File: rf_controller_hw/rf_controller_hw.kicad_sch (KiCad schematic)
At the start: 9 parts, among them J1 NRF24L01, SW1 SW_Push, SW10 JOYSTICK_BUTTON, SW2 SW_Push, SW3 SW_Push, SW4 SW_Push, SW8 SW_DIP_x05

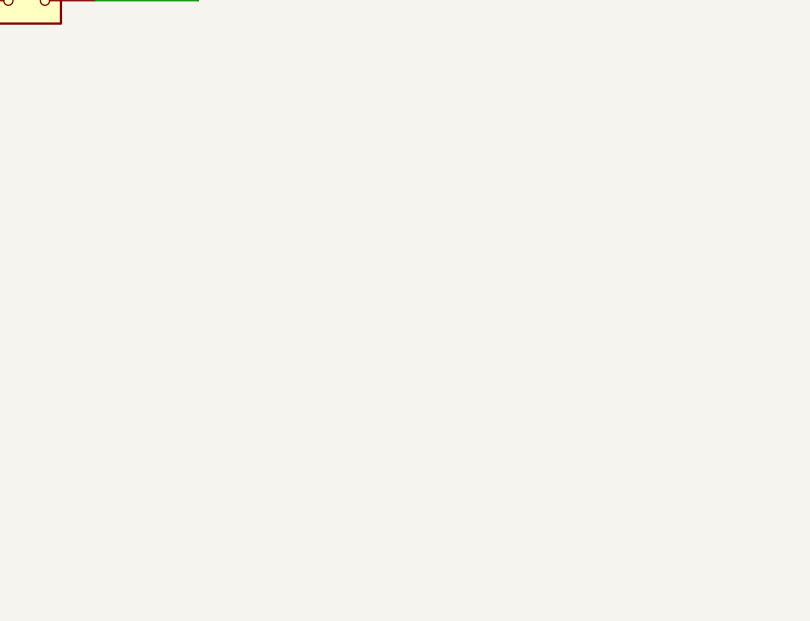
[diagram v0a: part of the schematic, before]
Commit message: Changed to mechanical keyboard switches
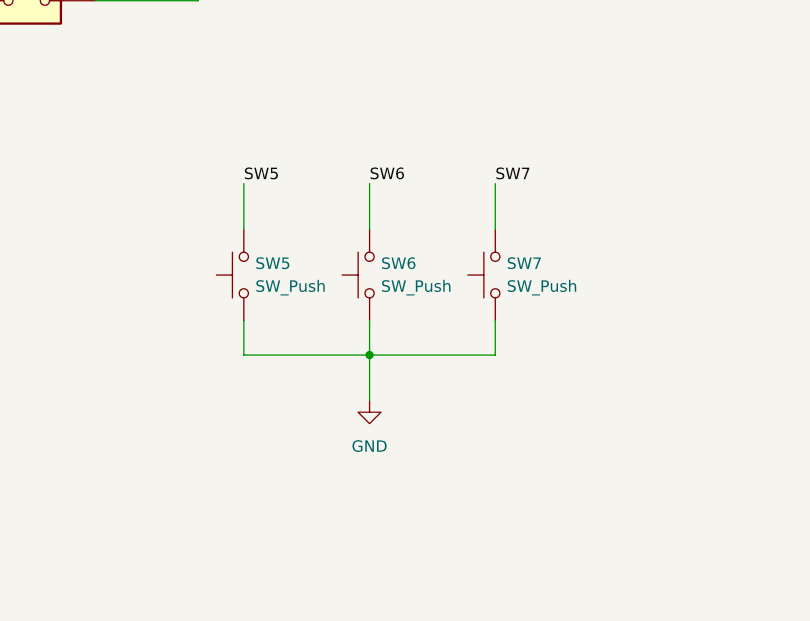
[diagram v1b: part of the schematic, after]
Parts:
- added SW5, SW6, SW7: SW_Push, Button_Switch_Keyboard:SW_Cherry_MX_1.00u_PCB, symbol Switch:SW_Push
- SW1, SW2, SW3, SW4: footprint (none) -> Button_Switch_Keyboard:SW_Cherry_MX_1.00u_PCB
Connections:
- net GND: now also SW5.1, SW6.1, SW7.1
- net SW5: now also SW5.2
- net SW6: now also SW6.2
- net SW7: now also SW7.2
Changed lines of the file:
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@@
   (junction (at 56.007 179.07) (diameter 0) (color 0 0 0 0)
+  )
+  (junction (at 171.45 143.51) (diameter 0) (color 0 0 0 0)
   )
   (junction (at 129.54 52.07) (diameter 0) (color 0 0 0 0)
@@
     (stroke (width 0) (type default) (color 0 0 0 0))
   )
+  (wire (pts (xy 171.45 143.51) (xy 185.42 143.51))
+    (stroke (width 0) (type default) (color 0 0 0 0))
+  )
   (wire (pts (xy 129.54 45.72) (xy 151.13 45.72))
     (stroke (width 0) (type default) (color 0 0 0 0))
@@
     (stroke (width 0) (type default) (color 0 0 0 0))
   )
+  (wire (pts (xy 171.45 139.7) (xy 171.45 143.51))
+    (stroke (width 0) (type default) (color 0 0 0 0))
+  )
   (wire (pts (xy 55.88 139.7) (xy 55.88 137.16))
     (stroke (width 0) (type default) (color 0 0 0 0))
@@
     (stroke (width 0) (type default) (color 0 0 0 0))
   )
+  (wire (pts (xy 185.42 124.46) (xy 185.42 129.54))
+    (stroke (width 0) (type default) (color 0 0 0 0))
+  )
   (wire (pts (xy 140.97 101.6) (xy 152.4 101.6))
     (stroke (width 0) (type default) (color 0 0 0 0))
@@
     (stroke (width 0) (type default) (color 0 0 0 0))
   )
+  (wire (pts (xy 185.42 143.51) (xy 185.42 139.7))
+    (stroke (width 0) (type default) (color 0 0 0 0))
+  )
   (wire (pts (xy 69.85 101.6) (xy 82.55 101.6))
     (stroke (width 0) (type default) (color 0 0 0 0))
@@
     (stroke (width 0) (type default) (color 0 0 0 0))
   )
+  (wire (pts (xy 171.45 148.59) (xy 171.45 143.51))
+    (stroke (width 0) (type default) (color 0 0 0 0))
+  )
   (wire (pts (xy 48.26 179.07) (xy 48.26 165.1))
     (stroke (width 0) (type default) (color 0 0 0 0))
@@
     (stroke (width 0) (type default) (color 0 0 0 0))
   )
+  (wire (pts (xy 157.48 124.46) (xy 157.48 129.54))
+    (stroke (width 0) (type default) (color 0 0 0 0))
+  )
   (wire (pts (xy 129.54 45.72) (xy 129.54 36.83))
     (stroke (width 0) (type default) (color 0 0 0 0))
@@
     (stroke (width 0) (type default) (color 0 0 0 0))
   )
+  (wire (pts (xy 171.45 143.51) (xy 157.48 143.51))
+    (stroke (width 0) (type default) (color 0 0 0 0))
+  )
   (wire (pts (xy 68.58 76.2) (xy 68.58 86.36))
     (stroke (width 0) (type default) (color 0 0 0 0))
@@
     (stroke (width 0) (type default) (color 0 0 0 0))
   )
+  (wire (pts (xy 157.48 143.51) (xy 157.48 139.7))
+    (stroke (width 0) (type default) (color 0 0 0 0))
+  )
   (wire (pts (xy 143.51 49.53) (xy 151.13 49.53))
     (stroke (width 0) (type default) (color 0 0 0 0))
@@
   )
   (wire (pts (xy 140.97 96.52) (xy 152.4 96.52))
+    (stroke (width 0) (type default) (color 0 0 0 0))
+  )
+  (wire (pts (xy 171.45 124.46) (xy 171.45 129.54))
     (stroke (width 0) (type default) (color 0 0 0 0))
   )
@@
     (effects (font (size 1.27 1.27)) (justify left bottom))
   )
+  (label "SW7" (at 185.42 124.46 0)
+    (effects (font (size 1.27 1.27)) (justify left bottom))
+  )
+  (label "SW6" (at 171.45 124.46 0)
+    (effects (font (size 1.27 1.27)) (justify left bottom))
+  )
   (label "SW4" (at 74.93 166.37 0)
     (effects (font (size 1.27 1.27)) (justify left bottom))
@@
   )
   (label "SW2" (at 74.93 151.13 0)
+    (effects (font (size 1.27 1.27)) (justify left bottom))
+  )
+  (label "SW5" (at 157.48 124.46 0)
     (effects (font (size 1.27 1.27)) (justify left bottom))
   )
@@
     (pin "1")
   )
+  (symbol (lib_id "Switch:SW_Push") (at 157.48 134.62 90) (unit 1)
+    (in_bom yes) (on_board yes)
+    (property "Reference" "SW5" (id 0) (at 158.75 133.3499 90)
+      (effects (font (size 1.27 1.27)) (justify right))
+    )
+    (property "Value" "SW_Push" (id 1) (at 158.75 135.8899 90)
+      (effects (font (size 1.27 1.27)) (justify right))
+    )
+    (property "Footprint" "Button_Switch_Keyboard:SW_Cherry_MX_1.00u_PCB" (id 2) (at 152.4 134.62 0)
+      (effects (font (size 1.27 1.27)) hide)
+    )
+    (property "Datasheet" "~" (id 3) (at 152.4 134.62 0)
+      (effects (font (size 1.27 1.27)) hide)
+    )
+    (pin "1")
+    (pin "2")
+  )
   (symbol (lib_id "Device:Battery") (at 238.76 92.71 0) (unit 1)
     (in_bom yes) (on_board yes) (fields_autoplaced)
@@
       (effects (font (size 1.27 1.27)) (justify right))
     )
-    (property "Footprint" "" (id 2) (at 50.8 172.72 0)
+    (property "Footprint" "Button_Switch_Keyboard:SW_Cherry_MX_1.00u_PCB" (id 2) (at 50.8 172.72 0)
       (effects (font (size 1.27 1.27)) hide)
     )
@@
       (effects (font (size 1.27 1.27)) (justify right))
     )
-    (property "Footprint" "" (id 2) (at 57.15 160.02 0)
+    (property "Footprint" "Button_Switch_Keyboard:SW_Cherry_MX_1.00u_PCB" (id 2) (at 57.15 160.02 0)
       (effects (font (size 1.27 1.27)) hide)
     )
@@
     (pin "1")
   )
+  (symbol (lib_id "power:GND") (at 171.45 148.59 0) (unit 1)
+    (in_bom yes) (on_board yes) (fields_autoplaced)
+    (property "Reference" "#PWR?" (id 0) (at 171.45 154.94 0)
+      (effects (font (size 1.27 1.27)) hide)
+    )
+    (property "Value" "GND" (id 1) (at 171.45 153.67 0))
+    (property "Footprint" "" (id 2) (at 171.45 148.59 0)
+      (effects (font (size 1.27 1.27)) hide)
+    )
+    (property "Datasheet" "" (id 3) (at 171.45 148.59 0)
+      (effects (font (size 1.27 1.27)) hide)
+    )
+    (pin "1")
+  )
   (symbol (lib_id "rf_controller_hw:JOYSTICK_BUTTON") (at 167.64 41.91 0) (unit 1)
     (in_bom yes) (on_board yes) (fields_autoplaced)
@@
     (pin "1")
   )
+  (symbol (lib_id "Switch:SW_Push") (at 185.42 134.62 90) (unit 1)
+    (in_bom yes) (on_board yes)
+    (property "Reference" "SW7" (id 0) (at 186.69 133.3499 90)
+      (effects (font (size 1.27 1.27)) (justify right))
+    )
+    (property "Value" "SW_Push" (id 1) (at 186.69 135.8899 90)
+      (effects (font (size 1.27 1.27)) (justify right))
+    )
+    (property "Footprint" "Button_Switch_Keyboard:SW_Cherry_MX_1.00u_PCB" (id 2) (at 180.34 134.62 0)
+      (effects (font (size 1.27 1.27)) hide)
+    )
+    (property "Datasheet" "~" (id 3) (at 180.34 134.62 0)
+      (effects (font (size 1.27 1.27)) hide)
+    )
+    (pin "1")
+    (pin "2")
+  )
   (symbol (lib_id "Switch:SW_Push") (at 48.26 160.02 90) (unit 1)
     (in_bom yes) (on_board yes) (fields_autoplaced)
@@
       (effects (font (size 1.27 1.27)) (justify right))
     )
-    (property "Footprint" "" (id 2) (at 43.18 160.02 0)
+    (property "Footprint" "Button_Switch_Keyboard:SW_Cherry_MX_1.00u_PCB" (id 2) (at 43.18 160.02 0)
       (effects (font (size 1.27 1.27)) hide)
     )
     (property "Datasheet" "~" (id 3) (at 43.18 160.02 0)
+      (effects (font (size 1.27 1.27)) hide)
+    )
+    (pin "1")
+    (pin "2")
+  )
+  (symbol (lib_id "Switch:SW_Push") (at 171.45 134.62 90) (unit 1)
+    (in_bom yes) (on_board yes)
+    (property "Reference" "SW6" (id 0) (at 172.72 133.3499 90)
+      (effects (font (size 1.27 1.27)) (justify right))
+    )
+    (property "Value" "SW_Push" (id 1) (at 172.72 135.8899 90)
+      (effects (font (size 1.27 1.27)) (justify right))
+    )
+    (property "Footprint" "Button_Switch_Keyboard:SW_Cherry_MX_1.00u_PCB" (id 2) (at 166.37 134.62 0)
+      (effects (font (size 1.27 1.27)) hide)
+    )
+    (property "Datasheet" "~" (id 3) (at 166.37 134.62 0)
       (effects (font (size 1.27 1.27)) hide)
     )
@@
       (effects (font (size 1.27 1.27)) (justify right))
     )
-    (property "Footprint" "" (id 2) (at 50.8 144.78 0)
+    (property "Footprint" "Button_Switch_Keyboard:SW_Cherry_MX_1.00u_PCB" (id 2) (at 50.8 144.78 0)
       (effects (font (size 1.27 1.27)) hide)
     )
@@
       (reference "#PWR0104") (unit 1) (value "GND") (footprint "")
     )
+    (path "/48c4ecda-abf3-4160-93bc-5239180efec7"
+      (reference "#PWR?") (unit 1) (value "GND") (footprint "")
+    )
     (path "/101bb346-25f4-4312-ac36-24a07e532eca"
       (reference "BT1") (unit 1) (value "Battery") (footprint "rf_controller_hw:2AA_BATTERY")
@@
     )
     (path "/97e21eaa-300c-42c6-8a5a-11b6cd9036eb"
-      (reference "SW1") (unit 1) (value "SW_Push") (footprint "")
+      (reference "SW1") (unit 1) (value "SW_Push") (footprint "Button_Switch_Keyboard:SW_Cherry_MX_1.00u_PCB")
     )
     (path "/811832fb-9434-4b8b-8daf-4885d7552e58"
-      (reference "SW2") (unit 1) (value "SW_Push") (footprint "")
+      (reference "SW2") (unit 1) (value "SW_Push") (footprint "Button_Switch_Keyboard:SW_Cherry_MX_1.00u_PCB")
     )
     (path "/1b67850b-a099-4671-90ab-6d2f986cb142"
-      (reference "SW3") (unit 1) (value "SW_Push") (footprint "")
+      (reference "SW3") (unit 1) (value "SW_Push") (footprint "Button_Switch_Keyboard:SW_Cherry_MX_1.00u_PCB")
     )
     (path "/10dc1afe-7b1d-4e27-ac36-71876411d5b9"
-      (reference "SW4") (unit 1) (value "SW_Push") (footprint "")
+      (reference "SW4") (unit 1) (value "SW_Push") (footprint "Button_Switch_Keyboard:SW_Cherry_MX_1.00u_PCB")
+    )
+    (path "/0f228d33-5293-46e5-aa6b-af327a95a055"
+      (reference "SW5") (unit 1) (value "SW_Push") (footprint "Button_Switch_Keyboard:SW_Cherry_MX_1.00u_PCB")
+    )
+    (path "/881ac59d-5f23-4328-9a26-61425ad74be0"
+      (reference "SW6") (unit 1) (value "SW_Push") (footprint "Button_Switch_Keyboard:SW_Cherry_MX_1.00u_PCB")
+    )
+    (path "/7eca3aab-c402-41ce-a461-b675056355b5"
+      (reference "SW7") (unit 1) (value "SW_Push") (footprint "Button_Switch_Keyboard:SW_Cherry_MX_1.00u_PCB")
     )
     (path "/691fef37-3035-4bf1-a7e9-ebb9530ca238"

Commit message: Finished first draft:
 - Spread out buttons on right
 - Added power switch
 - Added a budget logo
 - Added gerbers for PCB order
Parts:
- added SW10: SW_SPDT, Connector_PinHeader_2.54mm:PinHeader_1x03_P2.54mm_Vertical, symbol Switch:SW_SPDT
- SW1: renamed from SW2; footprint Button_Switch_Keyboard:SW_Cherry_MX_1.00u_PCB -> Button_Switch_THT:SW_PUSH_6mm_H5mm
- SW2: renamed from SW1; footprint Button_Switch_Keyboard:SW_Cherry_MX_1.00u_PCB -> Button_Switch_THT:SW_PUSH_6mm_H5mm
- SW3: renamed from SW4; footprint Button_Switch_Keyboard:SW_Cherry_MX_1.00u_PCB -> Button_Switch_THT:SW_PUSH_6mm_H5mm
- SW4: renamed from SW3; footprint Button_Switch_Keyboard:SW_Cherry_MX_1.00u_PCB -> Button_Switch_THT:SW_PUSH_6mm_H5mm
- SW6: renamed from SW5; footprint Button_Switch_Keyboard:SW_Cherry_MX_1.00u_PCB -> Button_Switch_THT:SW_PUSH_6mm_H5mm
- SW8: renamed from SW6; footprint Button_Switch_Keyboard:SW_Cherry_MX_1.00u_PCB -> Button_Switch_THT:SW_PUSH_6mm_H5mm
- SW9: renamed from SW7; footprint Button_Switch_Keyboard:SW_Cherry_MX_1.00u_PCB -> Button_Switch_THT:SW_PUSH_6mm_H5mm
- renumbered SW8 to SW5, SW10 to SW7
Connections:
- net +3V0: now also SW10.2 (B); no longer BT1.1 (+)
- net DIP1: now also RZ1.13 (GP12); no longer RZ1.17 (GP26)
- net DIP2: now also RZ1.14 (GP13); no longer RZ1.16 (GP15)
- net DIP4: now also RZ1.16 (GP15); no longer RZ1.14 (GP13)
- net DIP5: now also RZ1.17 (GP26); no longer RZ1.13 (GP12)
- new net BATT_NOSW: BT1.1 (+), SW10.1 (A)
- no-connect marks 2 -> 3
